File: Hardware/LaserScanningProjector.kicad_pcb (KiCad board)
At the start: 2 copper layers, 84.8 x 89.9 mm, 78 parts, among them J1 5V_IN, J10 MOTOR_Y, J11 LASER, J2 SWD, J3 UART, J4 USB_B, J5 LCD, J6 Micro_SD_Card_Det, J7 AUX, J8 HEADPHONES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

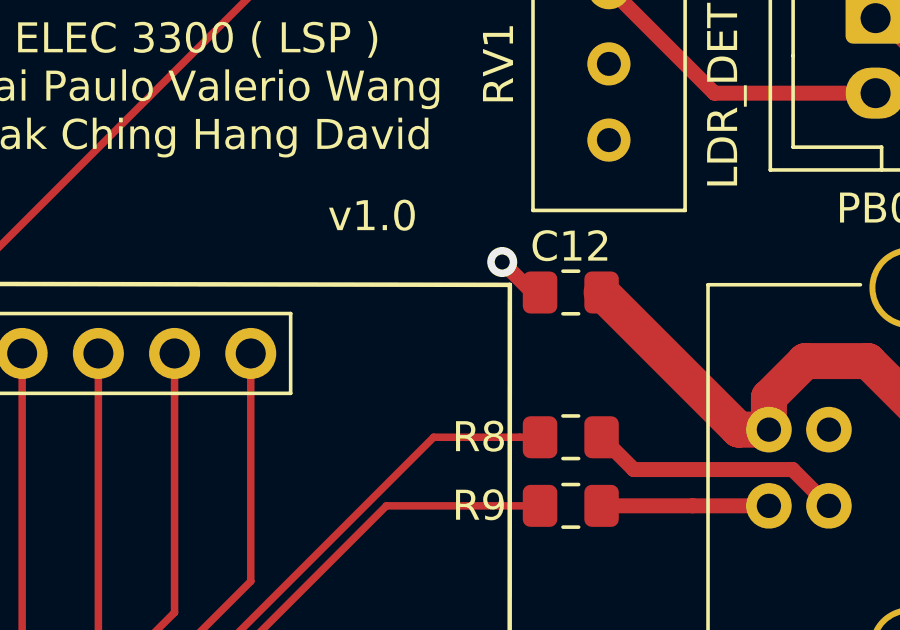
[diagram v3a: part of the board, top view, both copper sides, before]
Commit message: Add pull-up resistor to usb dp
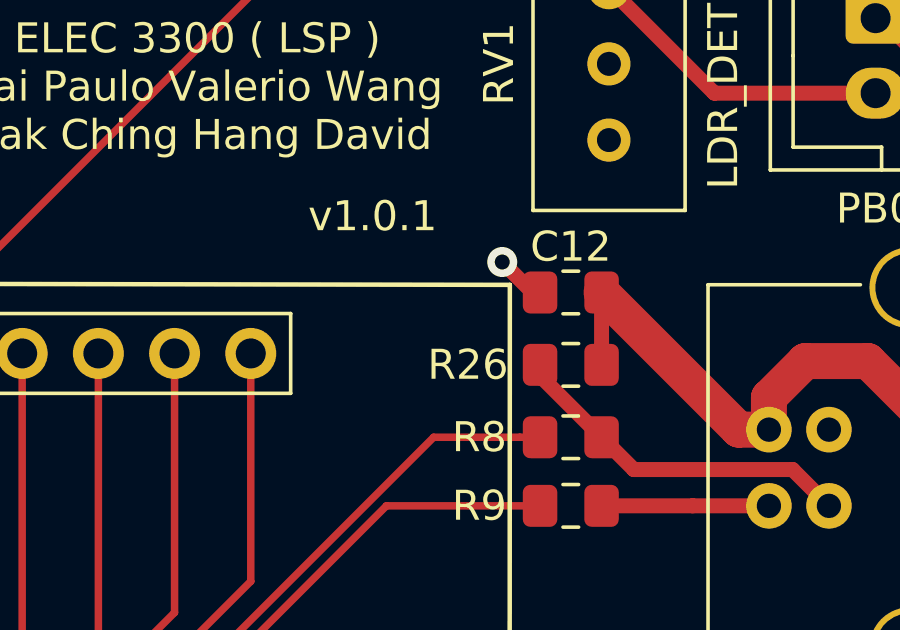
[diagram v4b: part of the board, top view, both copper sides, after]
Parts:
- added R26: 1k, Resistor_SMD:R_0805_2012Metric_Pad1.15x1.40mm_HandSolder, F.Cu at (128.0, 40.5)
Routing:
- net Net-(J4-Pad3): track 8.53 -> 11.8 mm
- net +5V: track 281.8 -> 284.2 mm
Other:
- board text added: "v1.0.1"
- board text removed: "v1.0"
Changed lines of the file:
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@@
-(kicad_pcb (version 20171130) (host pcbnew 5.1.4)
+(kicad_pcb (version 20171130) (host pcbnew 5.1.5)
   (general
     (thickness 1.6)
     (drawings 331)
-    (tracks 827)
+    (tracks 830)
     (zones 0)
-    (modules 78)
+    (modules 79)
     (nets 72)
   )
@@
   )
   (module Resistor_SMD:R_0805_2012Metric_Pad1.15x1.40mm_HandSolder (layer F.Cu)
+    (at 128.016 40.513 180)
+    (descr "Resistor SMD 0805 (2012 Metric), square (rectangular) end terminal, IPC_7351 nominal with elongated pad for handsoldering. (Body size source: https://docs.google.com/spreadsheets/d/1BsfQQcO9C6DZCsRaXUlFlo91Tg2WpOkGARC1WS5S8t0/edit?usp=sharing), generated with kicad-footprint-generator")
+    (tags "resistor handsolder")
+    (attr smd)
+    (fp_text reference R26 (at 3.429 0) (layer F.SilkS)
+      (effects (font (size 1 1) (thickness 0.15)))
+    )
+    (fp_text value 1k (at 0 1.65) (layer F.Fab)
+      (effects (font (size 1 1) (thickness 0.15)))
+    )
+    (fp_text user %R (at 0 0) (layer F.Fab)
+      (effects (font (size 0.5 0.5) (thickness 0.08)))
+    )
+    (fp_line (start 1.85 0.95) (end -1.85 0.95) (layer F.CrtYd) (width 0.05))
+    (fp_line (start 1.85 -0.95) (end 1.85 0.95) (layer F.CrtYd) (width 0.05))
+    (fp_line (start -1.85 -0.95) (end 1.85 -0.95) (layer F.CrtYd) (width 0.05))
+    (fp_line (start -1.85 0.95) (end -1.85 -0.95) (layer F.CrtYd) (width 0.05))
+    (fp_line (start -0.261252 0.71) (end 0.261252 0.71) (layer F.SilkS) (width 0.12))
+    (fp_line (start -0.261252 -0.71) (end 0.261252 -0.71) (layer F.SilkS) (width 0.12))
+    (fp_line (start 1 0.6) (end -1 0.6) (layer F.Fab) (width 0.1))
+    (fp_line (start 1 -0.6) (end 1 0.6) (layer F.Fab) (width 0.1))
+    (fp_line (start -1 -0.6) (end 1 -0.6) (layer F.Fab) (width 0.1))
+    (fp_line (start -1 0.6) (end -1 -0.6) (layer F.Fab) (width 0.1))
+    (pad 2 smd roundrect (at 1.025 0 180) (size 1.15 1.4) (layers F.Cu F.Paste F.Mask) (roundrect_rratio 0.217391)
+      (net 23 "Net-(J4-Pad3)"))
+    (pad 1 smd roundrect (at -1.025 0 180) (size 1.15 1.4) (layers F.Cu F.Paste F.Mask) (roundrect_rratio 0.217391)
+      (net 3 +5V))
+    (model ${KISYS3DMOD}/Resistor_SMD.3dshapes/R_0805_2012Metric.wrl
+      (at (xyz 0 0 0))
+      (scale (xyz 1 1 1))
+      (rotate (xyz 0 0 0))
+    )
+  )
+  (module Resistor_SMD:R_0805_2012Metric_Pad1.15x1.40mm_HandSolder (layer F.Cu)
     (at 132.588 96.012 270)
     (descr "Resistor SMD 0805 (2012 Metric), square (rectangular) end terminal, IPC_7351 nominal with elongated pad for handsoldering. (Body size source: https://docs.google.com/spreadsheets/d/1BsfQQcO9C6DZCsRaXUlFlo91Tg2WpOkGARC1WS5S8t0/edit?usp=sharing), generated with kicad-footprint-generator")
@@
     )
   )
-  (gr_text v1.0 (at 121.412 35.56) (layer F.SilkS)
+  (gr_text v1.0.1 (at 121.412 35.56) (layer F.SilkS)
     (effects (font (size 1 1) (thickness 0.15)))
   )
@@
   (segment (start 68.58 87.884) (end 68.58 66.548) (width 1.2) (layer F.Cu) (net 3))
   (segment (start 68.58 97.488) (end 68.58 87.884) (width 1.2) (layer F.Cu) (net 3))
+  (segment (start 129.041 40.513) (end 129.041 38.1) (width 0.5) (layer F.Cu) (net 3))
   (segment (start 96.885 29.981) (end 98.842 28.024) (width 0.5) (layer F.Cu) (net 4))
   (segment (start 96.012 29.981) (end 96.885 29.981) (width 0.5) (layer F.Cu) (net 4))
@@
   (segment (start 101.854 75.56641) (end 105.438 71.98241) (width 0.25) (layer F.Cu) (net 9))
   (segment (start 103.886 84.836) (end 101.854 82.804) (width 0.25) (layer F.Cu) (net 9))
-  (segment (start 130.048 92.973) (end 130.048 94.987) (width 0.7) (layer F.Cu) (net 12))
-  (segment (start 130.048 92.973) (end 129.02299 91.94799) (width 0.25) (layer F.Cu) (net 12))
-  (segment (start 117.493999 76.345999) (end 117.094 75.946) (width 0.25) (layer F.Cu) (net 12))
-  (segment (start 129.02299 87.87499) (end 117.493999 76.345999) (width 0.25) (layer F.Cu) (net 12))
-  (segment (start 129.02299 91.94799) (end 129.02299 87.87499) (width 0.25) (layer F.Cu) (net 12))
-  (via (at 117.094 75.946) (size 0.8) (drill 0.4) (layers F.Cu B.Cu) (net 12))
-  (segment (start 103.863 67.79) (end 103.0255 67.79) (width 0.25) (layer F.Cu) (net 12))
-  (via (at 111.506 70.104) (size 0.8) (drill 0.4) (layers F.Cu B.Cu) (net 12))
-  (segment (start 111.506 70.104) (end 110.236 70.104) (width 0.25) (layer B.Cu) (net 12))
-  (segment (start 110.236 70.104) (end 109.982 70.104) (width 0.25) (layer B.Cu) (net 12))
-  (via (at 104.902 68.326) (size 0.8) (drill 0.4) (layers F.Cu B.Cu) (net 12))
-  (segment (start 109.982 70.104) (end 108.204 68.326) (width 0.25) (layer B.Cu) (net 12))
-  (segment (start 108.204 68.326) (end 104.902 68.326) (width 0.25) (layer B.Cu) (net 12))
-  (segment (start 104.366 67.79) (end 103.0255 67.79) (width 0.25) (layer F.Cu) (net 12))
-  (segment (start 104.902 68.326) (end 104.366 67.79) (width 0.25) (layer F.Cu) (net 12))
-  (segment (start 117.094 75.946) (end 117.094 74.94864) (width 0.25) (layer B.Cu) (net 12))
-  (segment (start 114.906681 72.761321) (end 115.30668 73.16132) (width 0.25) (layer F.Cu) (net 12))
-  (segment (start 115.706679 73.561319) (end 115.30668 73.16132) (width 0.25) (layer B.Cu) (net 12))
-  (segment (start 112.24936 70.104) (end 114.906681 72.761321) (width 0.25) (layer F.Cu) (net 12))
-  (segment (start 117.094 74.94864) (end 115.706679 73.561319) (width 0.25) (layer B.Cu) (net 12))
-  (via (at 115.30668 73.16132) (size 0.8) (drill 0.4) (layers F.Cu B.Cu) (net 12))
-  (segment (start 111.506 70.104) (end 112.24936 70.104) (width 0.25) (layer F.Cu) (net 12))
-  (segment (start 106.938 73.41) (end 106.938 70.2025) (width 0.25) (layer F.Cu) (net 11))
-  (segment (start 110.036 76.2) (end 109.728 76.2) (width 0.25) (layer F.Cu) (net 11))
-  (segment (start 109.728 76.2) (end 106.938 73.41) (width 0.25) (layer F.Cu) (net 11))
-  (segment (start 109.728 76.508) (end 110.036 76.2) (width 0.25) (layer F.Cu) (net 11))
-  (segment (start 109.982 80.763) (end 109.982 76.508) (width 0.25) (layer F.Cu) (net 11))
   (segment (start 132.588 92.973) (end 132.588 94.488) (width 0.7) (layer F.Cu) (net 10))
   (via (at 117.851347 75.188653) (size 0.8) (drill 0.4) (layers F.Cu B.Cu) (net 10))
@@
   (segment (start 131.63619 92.973) (end 131.07301 92.40982) (width 0.25) (layer F.Cu) (net 10))
   (segment (start 104.915467 67.314161) (end 103.049661 67.314161) (width 0.25) (layer F.Cu) (net 10))
+  (segment (start 106.938 73.41) (end 106.938 70.2025) (width 0.25) (layer F.Cu) (net 11))
+  (segment (start 110.036 76.2) (end 109.728 76.2) (width 0.25) (layer F.Cu) (net 11))
+  (segment (start 109.728 76.2) (end 106.938 73.41) (width 0.25) (layer F.Cu) (net 11))
+  (segment (start 109.728 76.508) (end 110.036 76.2) (width 0.25) (layer F.Cu) (net 11))
+  (segment (start 109.982 80.763) (end 109.982 76.508) (width 0.25) (layer F.Cu) (net 11))
+  (segment (start 130.048 92.973) (end 130.048 94.987) (width 0.7) (layer F.Cu) (net 12))
+  (segment (start 130.048 92.973) (end 129.02299 91.94799) (width 0.25) (layer F.Cu) (net 12))
+  (segment (start 117.493999 76.345999) (end 117.094 75.946) (width 0.25) (layer F.Cu) (net 12))
+  (segment (start 129.02299 87.87499) (end 117.493999 76.345999) (width 0.25) (layer F.Cu) (net 12))
+  (segment (start 129.02299 91.94799) (end 129.02299 87.87499) (width 0.25) (layer F.Cu) (net 12))
+  (via (at 117.094 75.946) (size 0.8) (drill 0.4) (layers F.Cu B.Cu) (net 12))
+  (segment (start 103.863 67.79) (end 103.0255 67.79) (width 0.25) (layer F.Cu) (net 12))
+  (via (at 111.506 70.104) (size 0.8) (drill 0.4) (layers F.Cu B.Cu) (net 12))
+  (segment (start 111.506 70.104) (end 110.236 70.104) (width 0.25) (layer B.Cu) (net 12))
+  (segment (start 110.236 70.104) (end 109.982 70.104) (width 0.25) (layer B.Cu) (net 12))
+  (via (at 104.902 68.326) (size 0.8) (drill 0.4) (layers F.Cu B.Cu) (net 12))
+  (segment (start 109.982 70.104) (end 108.204 68.326) (width 0.25) (layer B.Cu) (net 12))
+  (segment (start 108.204 68.326) (end 104.902 68.326) (width 0.25) (layer B.Cu) (net 12))
+  (segment (start 104.366 67.79) (end 103.0255 67.79) (width 0.25) (layer F.Cu) (net 12))
+  (segment (start 104.902 68.326) (end 104.366 67.79) (width 0.25) (layer F.Cu) (net 12))
+  (segment (start 117.094 75.946) (end 117.094 74.94864) (width 0.25) (layer B.Cu) (net 12))
+  (segment (start 114.906681 72.761321) (end 115.30668 73.16132) (width 0.25) (layer F.Cu) (net 12))
+  (segment (start 115.706679 73.561319) (end 115.30668 73.16132) (width 0.25) (layer B.Cu) (net 12))
+  (segment (start 112.24936 70.104) (end 114.906681 72.761321) (width 0.25) (layer F.Cu) (net 12))
+  (segment (start 117.094 74.94864) (end 115.706679 73.561319) (width 0.25) (layer B.Cu) (net 12))
+  (via (at 115.30668 73.16132) (size 0.8) (drill 0.4) (layers F.Cu B.Cu) (net 12))
+  (segment (start 111.506 70.104) (end 112.24936 70.104) (width 0.25) (layer F.Cu) (net 12))
   (segment (start 88.746 108.204) (end 90.778 106.172) (width 0.6) (layer F.Cu) (net 13))
   (segment (start 87.296 108.204) (end 88.746 108.204) (width 0.6) (layer F.Cu) (net 13))
@@
   (segment (start 129.041 42.926) (end 130.116999 44.001999) (width 0.5) (layer F.Cu) (net 23))
   (segment (start 130.116999 44.001999) (end 135.409999 44.001999) (width 0.5) (layer F.Cu) (net 23))
+  (segment (start 126.991 40.876) (end 129.041 42.926) (width 0.5) (layer F.Cu) (net 23))
+  (segment (start 126.991 40.513) (end 126.991 40.876) (width 0.5) (layer F.Cu) (net 23))
   (segment (start 132.08 45.212) (end 129.041 45.212) (width 0.5) (layer F.Cu) (net 24))
   (segment (start 132.08 45.212) (end 134.62 45.212) (width 0.5) (layer F.Cu) (net 24))
